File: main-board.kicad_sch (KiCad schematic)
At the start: 0 parts

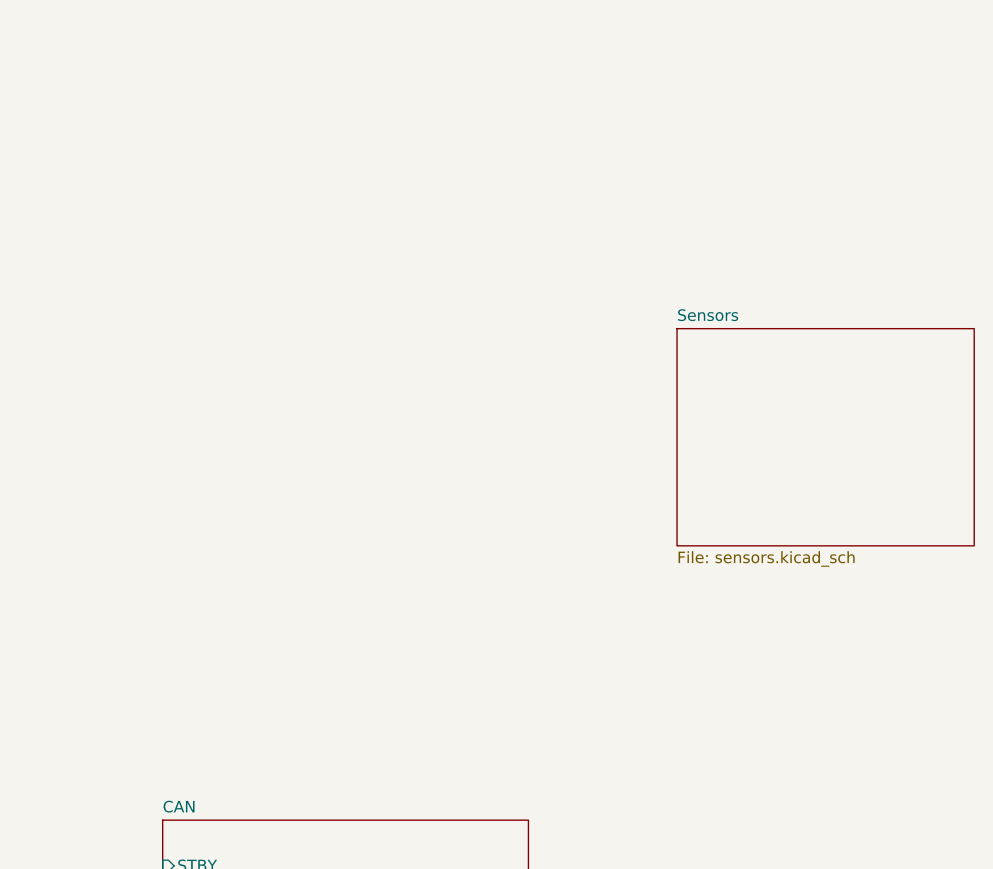
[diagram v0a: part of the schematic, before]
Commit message: Allocate GPIOs.
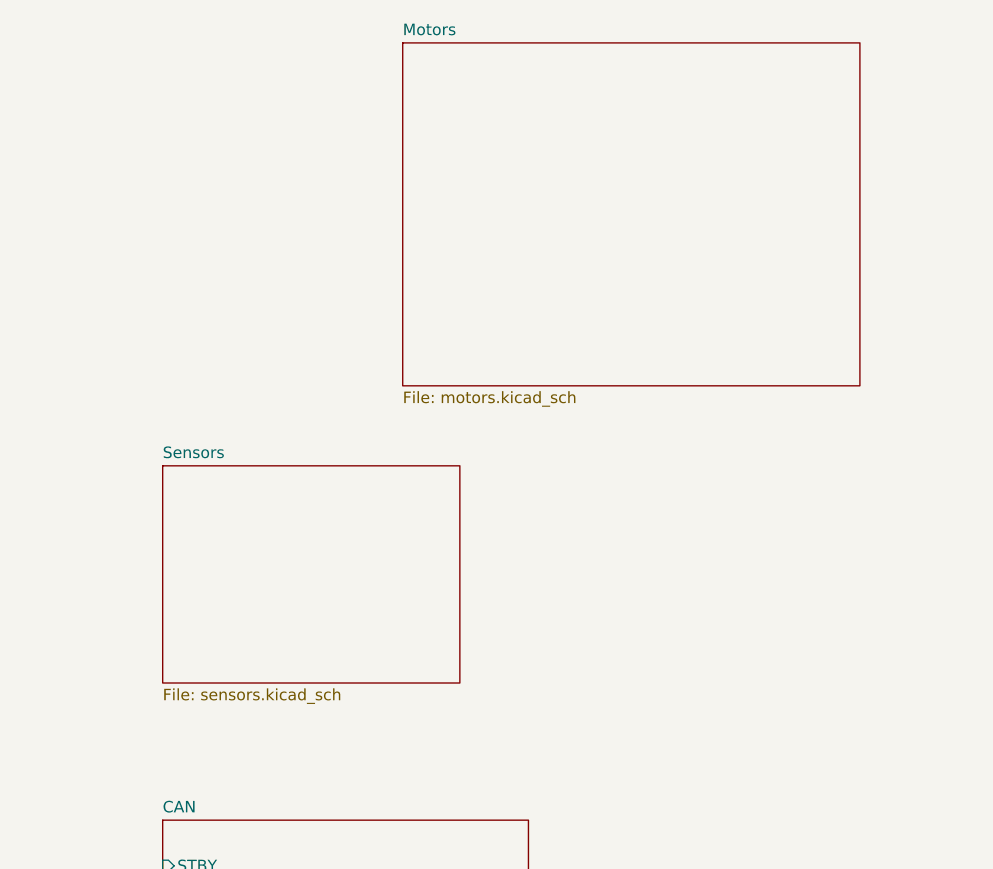
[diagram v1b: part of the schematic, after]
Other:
- added sheet Motors (motors.kicad_sch)
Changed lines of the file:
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@@
+    )
+  )
+  (sheet (at 180.34 36.83) (size 50.8 38.1) (fields_autoplaced)
+    (stroke (width 0.1524) (type solid))
+    (fill (color 0 0 0 0.0000))
+    (property "Sheetname" "Motors" (at 180.34 36.1184 0)
+      (effects (font (size 1.27 1.27)) (justify left bottom))
+    )
+    (property "Sheetfile" "motors.kicad_sch" (at 180.34 75.5146 0)
+      (effects (font (size 1.27 1.27)) (justify left top))
+    )
+    (instances
+      (project "main-board"
+        (path "/5ad67b7d-c56f-4b00-8953-cc84f90f9708" (page "11"))
+      )
     )
   )
@@
     )
   )
-  (sheet (at 210.82 68.58) (size 33.02 24.13) (fields_autoplaced)
+  (sheet (at 153.67 83.82) (size 33.02 24.13) (fields_autoplaced)
     (stroke (width 0.1524) (type solid))
     (fill (color 0 0 0 0.0000))
-    (property "Sheetname" "Sensors" (at 210.82 67.8684 0)
+    (property "Sheetname" "Sensors" (at 153.67 83.1084 0)
       (effects (font (size 1.27 1.27)) (justify left bottom))
     )
-    (property "Sheetfile" "sensors.kicad_sch" (at 210.82 93.2946 0)
+    (property "Sheetfile" "sensors.kicad_sch" (at 153.67 108.5346 0)
       (effects (font (size 1.27 1.27)) (justify left top))
     )

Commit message: Finish motor schematics.
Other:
- sheet Motors ports: added M1_CTRL_EN, M1_CTRL_STATUS, M1_DRV_FAULT, M2_CTRL_EN, M2_CTRL_STATUS, M2_DRV_FAULT, M3_CTRL_EN, M3_CTRL_STATUS, M3_DRV_FAULT, M4_CTRL_EN, M4_CTRL_STATUS, M4_DRV_FAULT, MD_CTRL_EN, MD_CTRL_STATUS, MD_DRV_FAULT, M_SPI_MISO, M_SPI_MOSI, M_SPI_SCK, ~{M1_CS_CTRL}, ~{M1_CS_DRV}, ~{M2_CS_CTRL}, ~{M2_CS_DRV}, ~{M3_CS_CTRL}, ~{M3_CS_DRV}, ~{M4_CS_CTRL}, ~{M4_CS_DRV}, ~{MD_CS_CTRL}, ~{MD_CS_DRV}; removed none

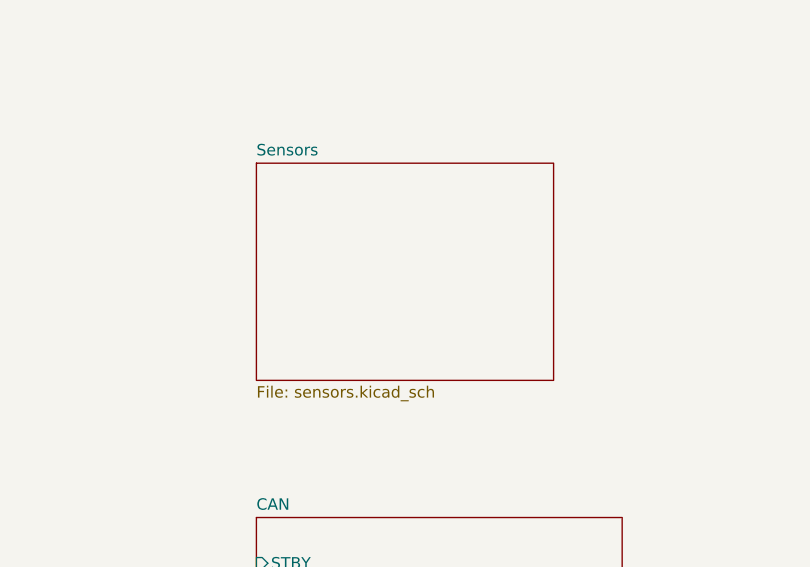
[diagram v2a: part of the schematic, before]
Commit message: Move sensors to one sheet.
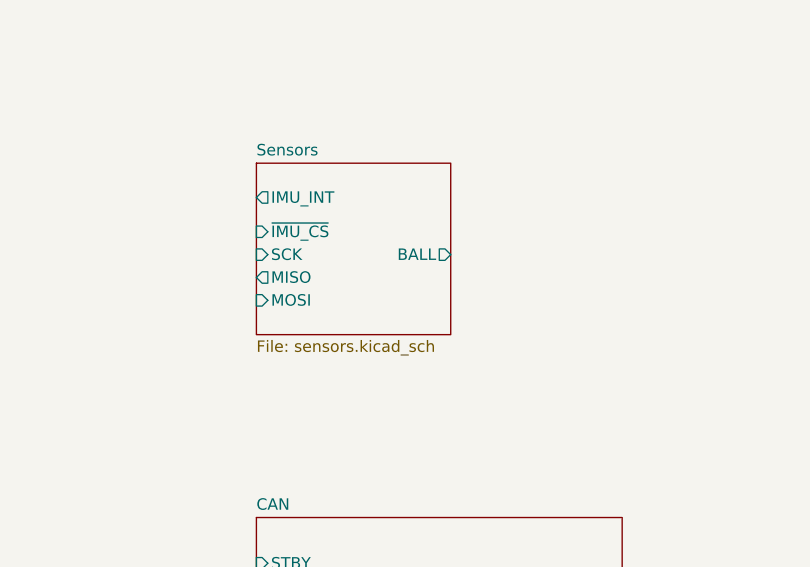
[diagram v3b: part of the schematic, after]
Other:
- sheet Sensors ports: added BALL, IMU_INT, MISO, MOSI, SCK, ~{IMU_CS}; removed none
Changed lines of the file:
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@@
     )
   )
-  (sheet (at 92.71 92.71) (size 33.02 24.13) (fields_autoplaced)
+  (sheet (at 92.71 92.71) (size 21.59 19.05) (fields_autoplaced)
     (stroke (width 0.1524) (type solid))
     (fill (color 0 0 0 0.0000))
@@
       (effects (font (size 1.27 1.27)) (justify left bottom))
     )
-    (property "Sheetfile" "sensors.kicad_sch" (at 92.71 117.4246 0)
+    (property "Sheetfile" "sensors.kicad_sch" (at 92.71 112.3446 0)
       (effects (font (size 1.27 1.27)) (justify left top))
     )
+    (pin "~{IMU_CS}" input (at 92.71 100.33 180)
+      (effects (font (size 1.27 1.27)) (justify left))
+    )
+    (pin "IMU_INT" output (at 92.71 96.52 180)
+      (effects (font (size 1.27 1.27)) (justify left))
+    )
+    (pin "MOSI" input (at 92.71 107.95 180)
+      (effects (font (size 1.27 1.27)) (justify left))
+    )
+    (pin "SCK" input (at 92.71 102.87 180)
+      (effects (font (size 1.27 1.27)) (justify left))
+    )
+    (pin "MISO" output (at 92.71 105.41 180)
+      (effects (font (size 1.27 1.27)) (justify left))
+    )
+    (pin "BALL" output (at 114.3 102.87 0)
+      (effects (font (size 1.27 1.27)) (justify right))
+    )
     (instances

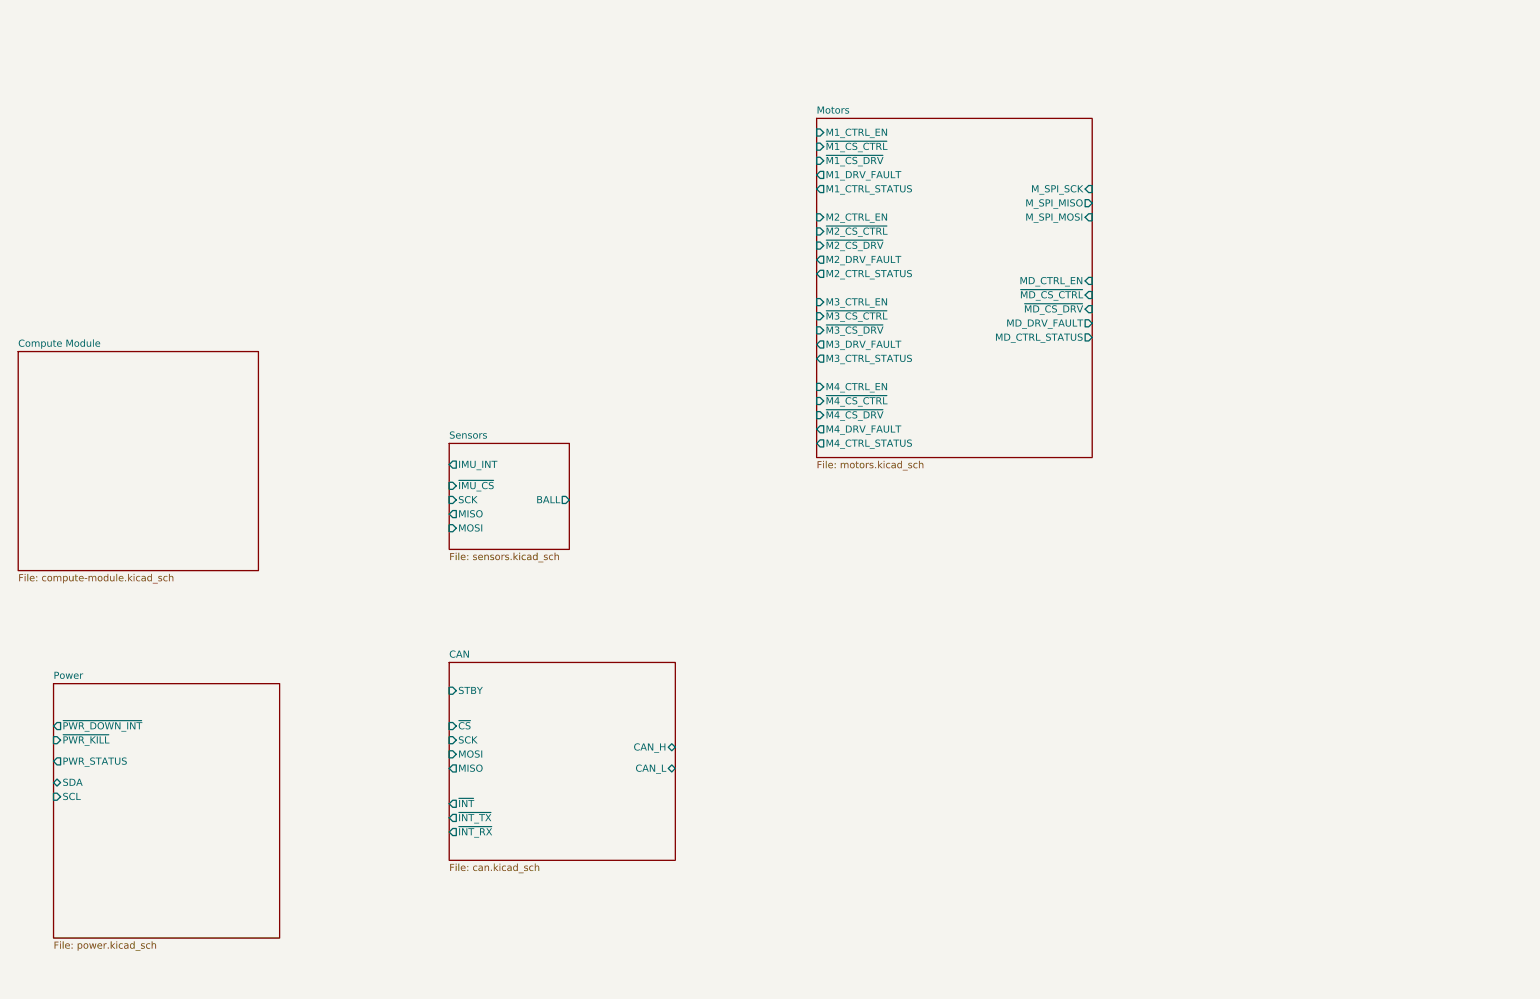
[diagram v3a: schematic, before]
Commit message: Unify CM4 sub-sheets.
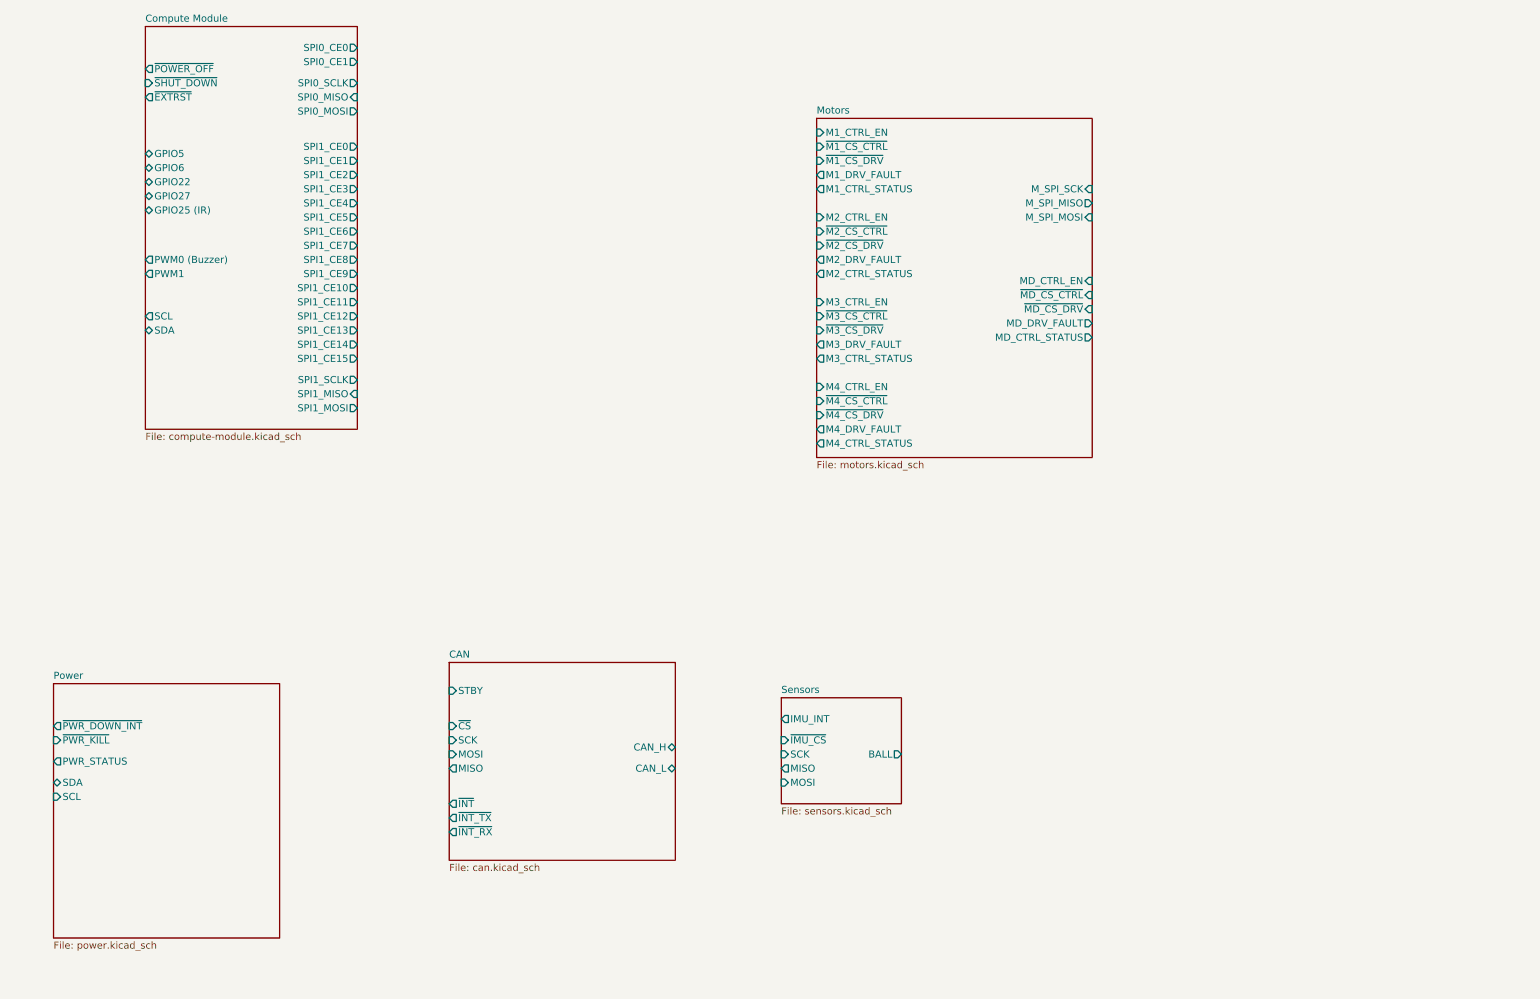
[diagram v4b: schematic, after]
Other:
- sheet Compute Module ports: added GPIO22, GPIO25 (IR), GPIO27, GPIO5, GPIO6, PWM0 (Buzzer), PWM1, SCL, SDA, SPI0_CE0, SPI0_CE1, SPI0_MISO, SPI0_MOSI, SPI0_SCLK, SPI1_CE0, SPI1_CE1, SPI1_CE10, SPI1_CE11, SPI1_CE12, SPI1_CE13, SPI1_CE14, SPI1_CE15, SPI1_CE2, SPI1_CE3, SPI1_CE4, SPI1_CE5, SPI1_CE6, SPI1_CE7, SPI1_CE8, SPI1_CE9, SPI1_MISO, SPI1_MOSI, SPI1_SCLK, ~{EXTRST}, ~{POWER_OFF}, ~{SHUT_DOWN}; removed none
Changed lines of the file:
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@@
     )
   )
-  (sheet (at 15.24 76.2) (size 43.18 39.37) (fields_autoplaced)
+  (sheet (at 38.1 17.78) (size 38.1 72.39) (fields_autoplaced)
     (stroke (width 0.1524) (type solid))
     (fill (color 0 0 0 0.0000))
-    (property "Sheetname" "Compute Module" (at 15.24 75.4884 0)
+    (property "Sheetname" "Compute Module" (at 38.1 17.0684 0)
       (effects (font (size 1.27 1.27)) (justify left bottom))
     )
-    (property "Sheetfile" "compute-module.kicad_sch" (at 15.24 116.1546 0)
+    (property "Sheetfile" "compute-module.kicad_sch" (at 38.1 90.7546 0)
       (effects (font (size 1.27 1.27)) (justify left top))
+    )
+    (pin "GPIO5" bidirectional (at 38.1 40.64 180)
+      (effects (font (size 1.27 1.27)) (justify left))
+    )
+    (pin "PWM1" output (at 38.1 62.23 180)
+      (effects (font (size 1.27 1.27)) (justify left))
+    )
+    (pin "GPIO6" bidirectional (at 38.1 43.18 180)
+      (effects (font (size 1.27 1.27)) (justify left))
+    )
+    (pin "~{POWER_OFF}" output (at 38.1 25.4 180)
+      (effects (font (size 1.27 1.27)) (justify left))
+    )
+    (pin "SPI1_MISO" input (at 76.2 83.82 0)
+      (effects (font (size 1.27 1.27)) (justify right))
+    )
+    (pin "GPIO22" bidirectional (at 38.1 45.72 180)
+      (effects (font (size 1.27 1.27)) (justify left))
+    )
+    (pin "SPI0_SCLK" output (at 76.2 27.94 0)
+      (effects (font (size 1.27 1.27)) (justify right))
+    )
+    (pin "SPI0_MISO" input (at 76.2 30.48 0)
+      (effects (font (size 1.27 1.27)) (justify right))
+    )
+    (pin "SCL" output (at 38.1 69.85 180)
+      (effects (font (size 1.27 1.27)) (justify left))
+    )
+    (pin "SDA" bidirectional (at 38.1 72.39 180)
+      (effects (font (size 1.27 1.27)) (justify left))
+    )
+    (pin "~{SHUT_DOWN}" input (at 38.1 27.94 180)
+      (effects (font (size 1.27 1.27)) (justify left))
+    )
+    (pin "SPI0_MOSI" output (at 76.2 33.02 0)
+      (effects (font (size 1.27 1.27)) (justify right))
+    )
+    (pin "GPIO27" bidirectional (at 38.1 48.26 180)
+      (effects (font (size 1.27 1.27)) (justify left))
+    )
+    (pin "GPIO25 (IR)" bidirectional (at 38.1 50.8 180)
+      (effects (font (size 1.27 1.27)) (justify left))
+    )
+    (pin "SPI0_CE0" output (at 76.2 21.59 0)
+      (effects (font (size 1.27 1.27)) (justify right))
+    )
+    (pin "PWM0 (Buzzer)" output (at 38.1 59.69 180)
+      (effects (font (size 1.27 1.27)) (justify left))
+    )
+    (pin "SPI0_CE1" output (at 76.2 24.13 0)
+      (effects (font (size 1.27 1.27)) (justify right))
+    )
+    (pin "SPI1_SCLK" output (at 76.2 81.28 0)
+      (effects (font (size 1.27 1.27)) (justify right))
+    )
+    (pin "SPI1_MOSI" output (at 76.2 86.36 0)
+      (effects (font (size 1.27 1.27)) (justify right))
+    )
+    (pin "SPI1_CE1" output (at 76.2 41.91 0)
+      (effects (font (size 1.27 1.27)) (justify right))
+    )
+    (pin "SPI1_CE3" output (at 76.2 46.99 0)
+      (effects (font (size 1.27 1.27)) (justify right))
+    )
+    (pin "SPI1_CE2" output (at 76.2 44.45 0)
+      (effects (font (size 1.27 1.27)) (justify right))
+    )
+    (pin "SPI1_CE0" output (at 76.2 39.37 0)
+      (effects (font (size 1.27 1.27)) (justify right))
+    )
+    (pin "SPI1_CE5" output (at 76.2 52.07 0)
+      (effects (font (size 1.27 1.27)) (justify right))
+    )
+    (pin "SPI1_CE4" output (at 76.2 49.53 0)
+      (effects (font (size 1.27 1.27)) (justify right))
+    )
+    (pin "SPI1_CE6" output (at 76.2 54.61 0)
+      (effects (font (size 1.27 1.27)) (justify right))
+    )
+    (pin "SPI1_CE7" output (at 76.2 57.15 0)
+      (effects (font (size 1.27 1.27)) (justify right))
+    )
+    (pin "~{EXTRST}" output (at 38.1 30.48 180)
+      (effects (font (size 1.27 1.27)) (justify left))
+    )
+    (pin "SPI1_CE10" output (at 76.2 64.77 0)
+      (effects (font (size 1.27 1.27)) (justify right))
+    )
+    (pin "SPI1_CE9" output (at 76.2 62.23 0)
+      (effects (font (size 1.27 1.27)) (justify right))
+    )
+    (pin "SPI1_CE8" output (at 76.2 59.69 0)
+      (effects (font (size 1.27 1.27)) (justify right))
+    )
+    (pin "SPI1_CE14" output (at 76.2 74.93 0)
+      (effects (font (size 1.27 1.27)) (justify right))
+    )
+    (pin "SPI1_CE11" output (at 76.2 67.31 0)
+      (effects (font (size 1.27 1.27)) (justify right))
+    )
+    (pin "SPI1_CE12" output (at 76.2 69.85 0)
+      (effects (font (size 1.27 1.27)) (justify right))
+    )
+    (pin "SPI1_CE15" output (at 76.2 77.47 0)
+      (effects (font (size 1.27 1.27)) (justify right))
+    )
+    (pin "SPI1_CE13" output (at 76.2 72.39 0)
+      (effects (font (size 1.27 1.27)) (justify right))
     )
     (instances
@@
     )
   )
-  (sheet (at 92.71 92.71) (size 21.59 19.05) (fields_autoplaced)
+  (sheet (at 152.4 138.43) (size 21.59 19.05) (fields_autoplaced)
     (stroke (width 0.1524) (type solid))
     (fill (color 0 0 0 0.0000))
-    (property "Sheetname" "Sensors" (at 92.71 91.9984 0)
+    (property "Sheetname" "Sensors" (at 152.4 137.7184 0)
       (effects (font (size 1.27 1.27)) (justify left bottom))
     )
-    (property "Sheetfile" "sensors.kicad_sch" (at 92.71 112.3446 0)
+    (property "Sheetfile" "sensors.kicad_sch" (at 152.4 158.0646 0)
       (effects (font (size 1.27 1.27)) (justify left top))
     )
-    (pin "~{IMU_CS}" input (at 92.71 100.33 180)
+    (pin "~{IMU_CS}" input (at 152.4 146.05 180)
       (effects (font (size 1.27 1.27)) (justify left))
     )
-    (pin "IMU_INT" output (at 92.71 96.52 180)
+    (pin "IMU_INT" output (at 152.4 142.24 180)
       (effects (font (size 1.27 1.27)) (justify left))
     )
-    (pin "MOSI" input (at 92.71 107.95 180)
+    (pin "MOSI" input (at 152.4 153.67 180)
       (effects (font (size 1.27 1.27)) (justify left))
     )
-    (pin "SCK" input (at 92.71 102.87 180)
+    (pin "SCK" input (at 152.4 148.59 180)
       (effects (font (size 1.27 1.27)) (justify left))
     )
-    (pin "MISO" output (at 92.71 105.41 180)
+    (pin "MISO" output (at 152.4 151.13 180)
       (effects (font (size 1.27 1.27)) (justify left))
     )
-    (pin "BALL" output (at 114.3 102.87 0)
+    (pin "BALL" output (at 173.99 148.59 0)
       (effects (font (size 1.27 1.27)) (justify right))
     )
